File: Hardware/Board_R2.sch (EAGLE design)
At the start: 53 parts, among them U1 EDISON_CONNECTOR_FULLMOUNTING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, U2 LAN9512-JZX, U3 MAX4995AAUT+, U4 EDISON_CONNECTOR_FULLHEADER, X1 J1011F01P

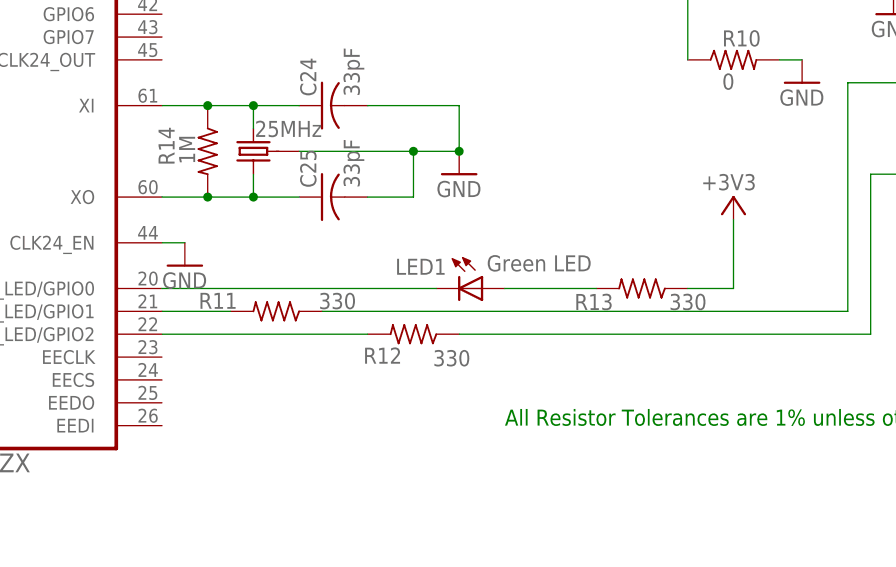
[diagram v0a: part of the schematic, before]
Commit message: Added intitial 4 layer board layout and made very minor changes to Schematic and BOM.
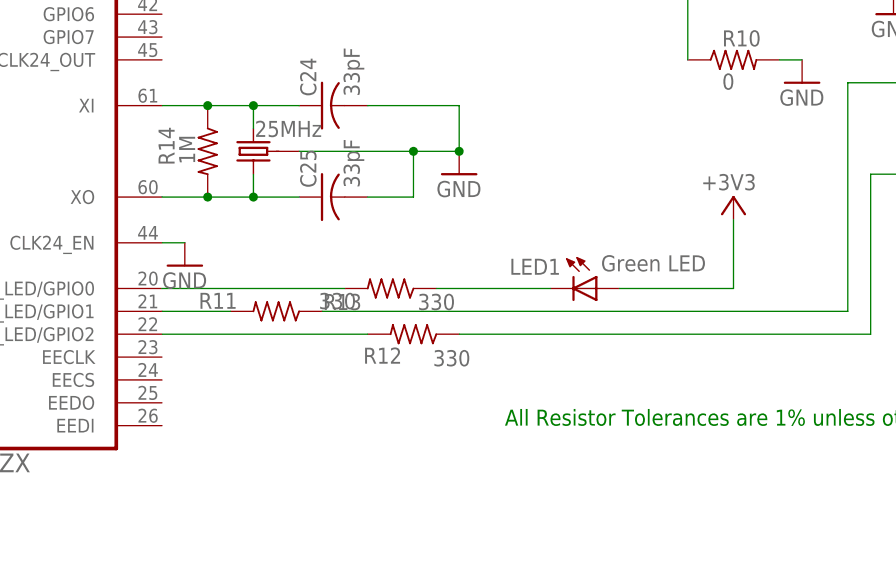
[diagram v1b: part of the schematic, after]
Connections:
- net N$11 renamed RX_P
- net N$12 renamed RX_N
- net N$13 renamed TX_N
- net N$14 renamed TX_P
- net N$24 renamed DSUSB_N
- net N$5 renamed DSUSB_P
- net +3V3: now also LED1.A; no longer R13.1
- net N$19: now also R13.1; no longer U2.NFDX_LED/GPIO0
- net N$20: now also U2.NFDX_LED/GPIO0; no longer LED1.A
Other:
- moved on the sheet: LED1, R13
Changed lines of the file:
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@@
 <attribute name="VALUE" x="323.85" y="102.362" size="1.778" layer="96" rot="R180"/>
 </instance>
-<instance part="LED1" gate="G$1" x="325.12" y="109.22" smashed="yes" rot="R270">
-<attribute name="NAME" x="315.468" y="110.744" size="1.778" layer="95"/>
-<attribute name="VALUE" x="325.628" y="111.125" size="1.778" layer="96"/>
+<instance part="LED1" gate="G$1" x="337.82" y="109.22" smashed="yes" rot="R270">
+<attribute name="NAME" x="328.168" y="110.744" size="1.778" layer="95"/>
+<attribute name="VALUE" x="338.328" y="111.125" size="1.778" layer="96"/>
 </instance>
-<instance part="R13" gate="G$1" x="342.9" y="109.22" smashed="yes" rot="R180">
-<attribute name="NAME" x="339.6996" y="108.6104" size="1.778" layer="95" rot="R180"/>
-<attribute name="VALUE" x="350.0882" y="108.6104" size="1.778" layer="96" rot="R180"/>
+<instance part="R13" gate="G$1" x="314.96" y="109.22" smashed="yes" rot="R180">
+<attribute name="NAME" x="311.7596" y="108.6104" size="1.778" layer="95" rot="R180"/>
+<attribute name="VALUE" x="322.1482" y="108.6104" size="1.778" layer="96" rot="R180"/>
 </instance>
 <instance part="+3V9" gate="G$1" x="353.06" y="119.38" smashed="yes">
@@
 </segment>
 <segment>
-<pinref part="R13" gate="G$1" pin="1"/>
 <pinref part="+3V9" gate="G$1" pin="+3V3"/>
-<wire x1="347.98" y1="109.22" x2="353.06" y2="109.22" width="0.1524" layer="91"/>
 <wire x1="353.06" y1="109.22" x2="353.06" y2="116.84" width="0.1524" layer="91"/>
+<pinref part="LED1" gate="G$1" pin="A"/>
+<wire x1="340.36" y1="109.22" x2="353.06" y2="109.22" width="0.1524" layer="91"/>
 </segment>
 <segment>
@@
 </segment>
 </net>
-<net name="N$11" class="0">
+<net name="RX_P" class="0">
 <segment>
 <pinref part="U2" gate="A" pin="RXN"/>
@@
 </segment>
 </net>
-<net name="N$13" class="0">
+<net name="TX_N" class="0">
 <segment>
 <pinref part="U2" gate="A" pin="TXN"/>
@@
 </segment>
 </net>
-<net name="N$14" class="0">
+<net name="TX_P" class="0">
 <segment>
 <pinref part="U2" gate="A" pin="TXP"/>
@@
 </segment>
 </net>
-<net name="N$12" class="0">
+<net name="RX_N" class="0">
 <segment>
 <pinref part="U2" gate="A" pin="RXP"/>
@@
 </segment>
 </net>
-<net name="N$19" class="0">
-<segment>
-<pinref part="LED1" gate="G$1" pin="C"/>
-<pinref part="U2" gate="A" pin="NFDX_LED/GPIO0"/>
-<wire x1="320.04" y1="109.22" x2="289.56" y2="109.22" width="0.1524" layer="91"/>
-</segment>
-</net>
-<net name="N$20" class="0">
-<segment>
-<pinref part="LED1" gate="G$1" pin="A"/>
-<pinref part="R13" gate="G$1" pin="2"/>
-<wire x1="327.66" y1="109.22" x2="337.82" y2="109.22" width="0.1524" layer="91"/>
-</segment>
-</net>
 <net name="N$21" class="0">
 <segment>
@@
 </segment>
 </net>
-<net name="N$5" class="0">
+<net name="DSUSB_P" class="0">
 <segment>
 <wire x1="401.32" y1="246.38" x2="312.42" y2="246.38" width="0.1524" layer="91"/>
@@
 </segment>
 </net>
-<net name="N$24" class="0">
+<net name="DSUSB_N" class="0">
 <segment>
 <pinref part="U2" gate="A" pin="USBDM2"/>
@@
 </segment>
 </net>
+<net name="N$19" class="0">
+<segment>
+<pinref part="LED1" gate="G$1" pin="C"/>
+<pinref part="R13" gate="G$1" pin="1"/>
+<wire x1="332.74" y1="109.22" x2="320.04" y2="109.22" width="0.1524" layer="91"/>
+</segment>
+</net>
+<net name="N$20" class="0">
+<segment>
+<pinref part="U2" gate="A" pin="NFDX_LED/GPIO0"/>
+<pinref part="R13" gate="G$1" pin="2"/>
+<wire x1="289.56" y1="109.22" x2="309.88" y2="109.22" width="0.1524" layer="91"/>
+</segment>
+</net>

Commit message: Updated board and schematic as per recommendations.
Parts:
- removed JP1: (no value), jumper:JP2Q
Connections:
- net N$1 renamed VDD18USBPLL
- net N$2 renamed VDD18ETHPLL
- net N$4 renamed VDD18CORE
- net USBUP: no longer JP1.3, U1.USB_DP
- net USBUP2: no longer JP1.1, U1.USB_DN
- net USBUPDN: now also U1.USB_DN; no longer JP1.2
- net USBUPDP: now also U1.USB_DP; no longer JP1.4
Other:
- note added: "2.1"
- note added: "Removed Solder Jumper and cleaned schematic"
- note removed: "2"
- note removed: "Removed one downstream USB port and changed downstream power control"
- moved on the sheet: C1, C10, C11, C12, C13, C14, C15, C16, C17, C2, C3, C4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

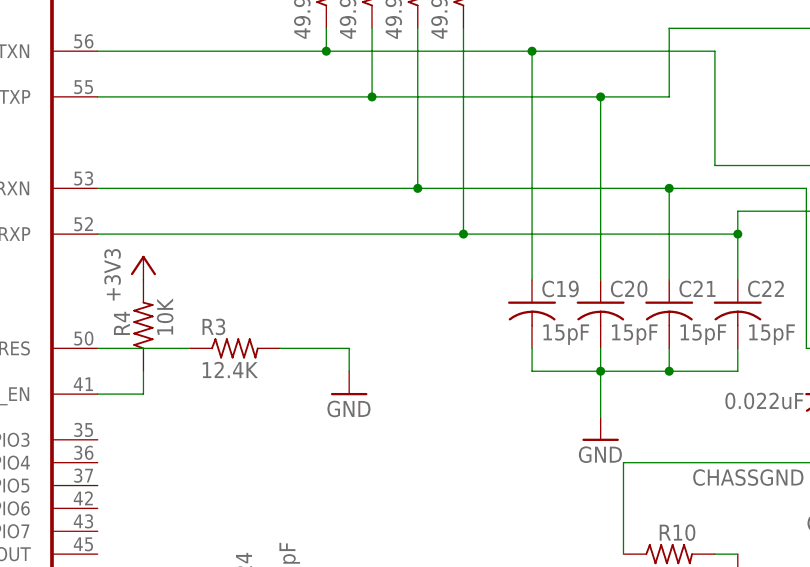
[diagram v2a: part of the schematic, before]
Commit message: Removed olf board file, made some changes to new board file and schematic. BOM is till complete.
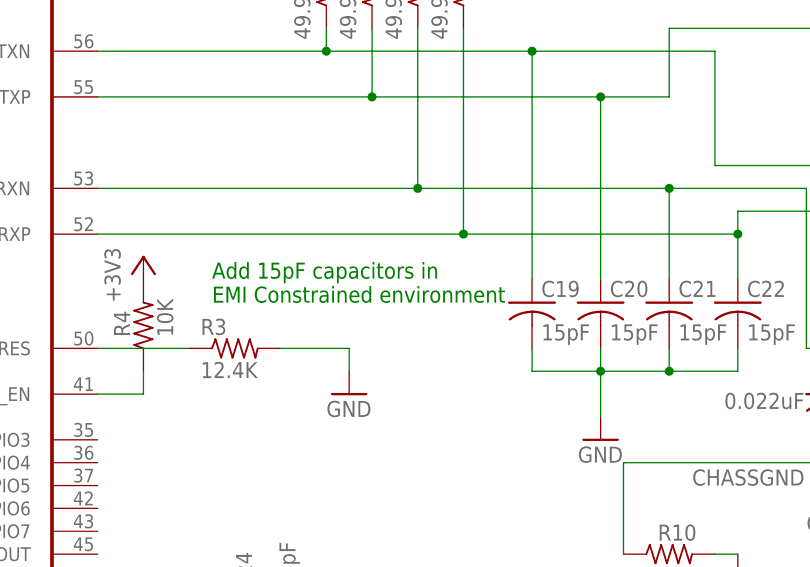
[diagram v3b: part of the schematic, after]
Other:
- note added: "Add 15pF capacitors in EMI Constrained environment"
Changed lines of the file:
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@@
 <text x="327.66" y="7.62" size="1.778" layer="91">Removed Solder Jumper and cleaned schematic</text>
 <text x="327.406" y="11.176" size="2.54" layer="91">---------------------------------------REVISION NOTES</text>
+<text x="302.26" y="162.56" size="1.778" layer="91">Add 15pF capacitors in
+EMI Constrained environment</text>
 </plain>
 <instances>
@@
 </schematic>
 </drawing>
+<compatibility>
+<note version="6.3" minversion="6.2.2" severity="warning">
+Since Version 6.2.2 text objects can contain more than one line,
+which will not be processed correctly with this version.
+</note>
+</compatibility>
 </eagle>

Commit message: Board ready for manufacturing: Added mounting hardware and verified trace impedances. Designed to Advanced Circuit's specifications and passes their checks at FreeDFM.com.
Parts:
- added R17: 10K, resistor:R-US_R0603
- added TP1, TP2: TPTP20R, testpad:TPTP20R
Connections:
- net USBUPDN renamed USB_UP_N
- net USBUPDP renamed USB_UP_P
- new net CLK24_OUT: TP1.TP, U2.CLK24_OUT
- new net N$1: R17.1, U2.CLK24_EN
- net +3V3: now also R17.2
- net GND: now also TP2.TP, U1.USB_ID; no longer U2.CLK24_EN
- net P3: no longer U1.USB_ID
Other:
- note added: "All connections pass-through to bottom connector EXCEPT Upstream USB (USB_ID, USB_VBUS, USB_UP_P, USB_UP_N)"
- note added: "Fixed USB_ID and added test points"
- note removed: "1"
- note removed: "Removed Solder Jumper and cleaned schematic"
- moved on the sheet: R3, R4
